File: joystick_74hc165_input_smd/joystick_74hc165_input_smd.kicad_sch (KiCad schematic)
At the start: 19 parts, among them J1 Conn_01x18, J2 Conn_02x14_Odd_Even

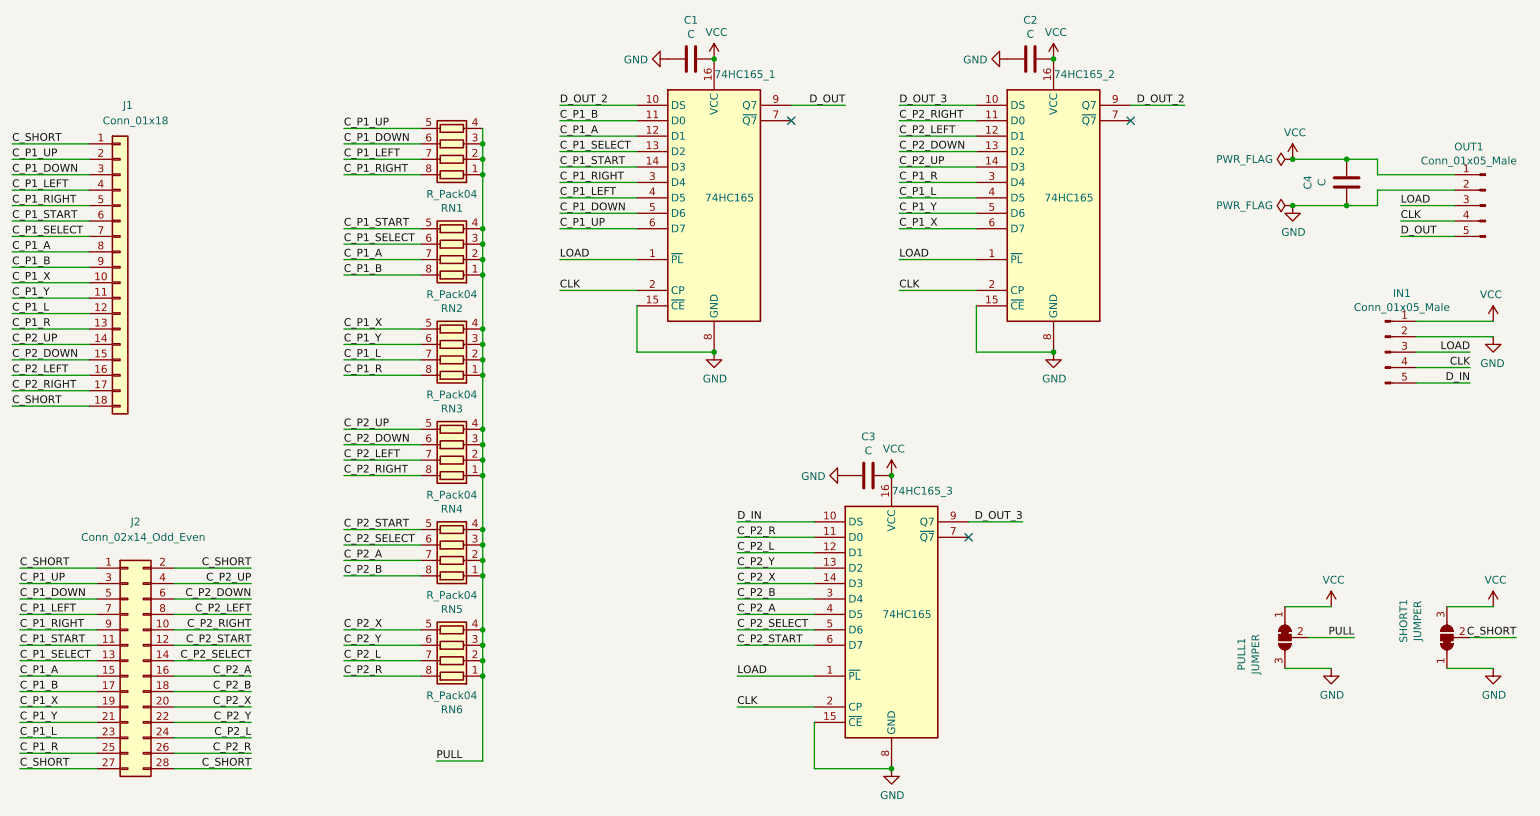
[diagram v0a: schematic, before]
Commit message: 부품 값 입력
Signed-off-by: Ju, Gyeong-min <jcmh74@gmail.com>
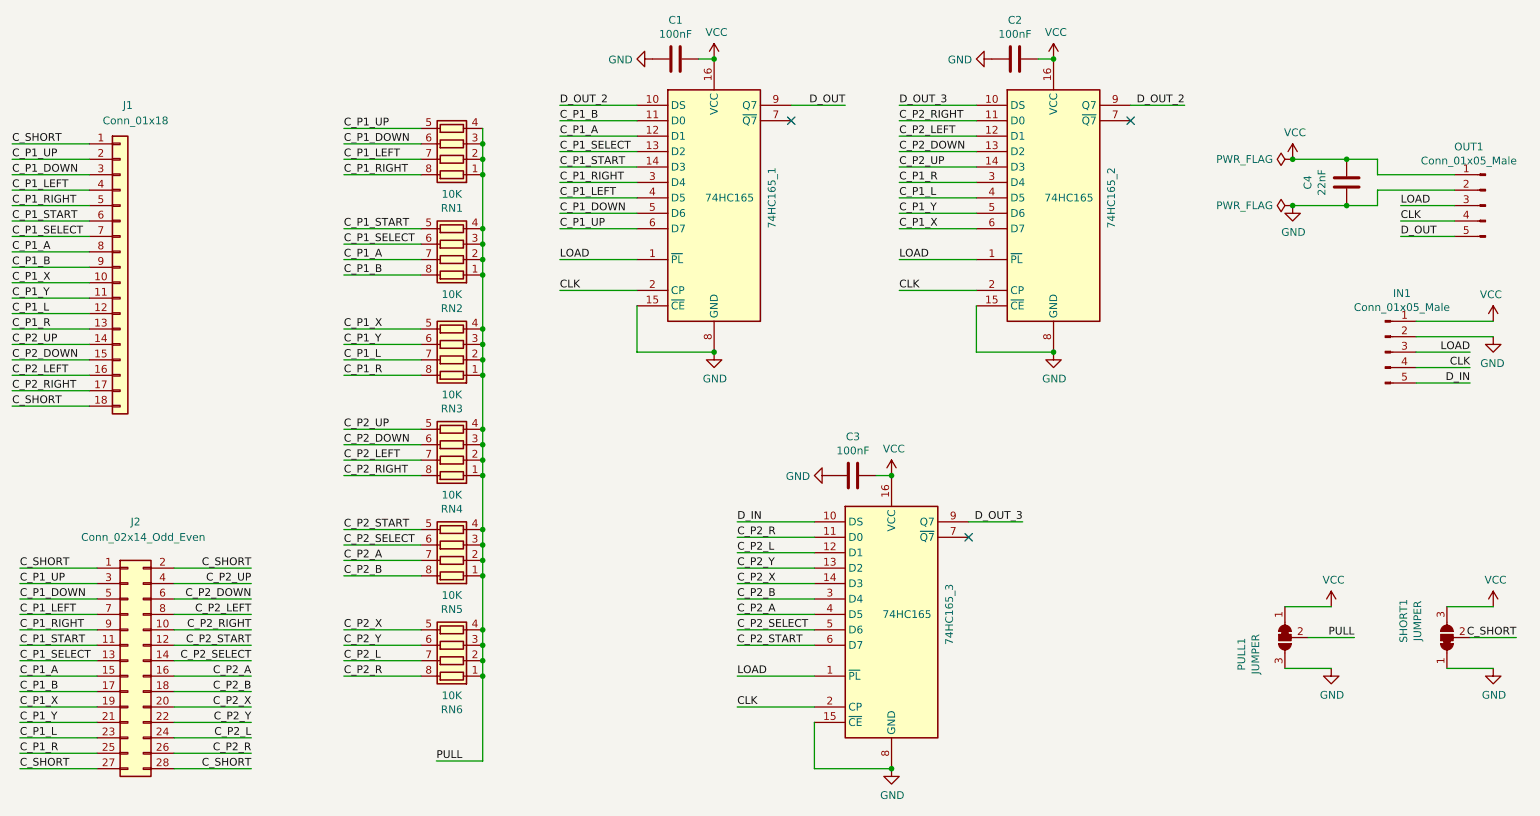
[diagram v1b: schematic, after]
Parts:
- C1, C2, C3: value C -> 100nF
- C4: value C -> 22nF
- RN1, RN2, RN3, RN4, RN5, RN6: value R_Pack04 -> 10K
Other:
- moved on the sheet: C1, C2, C3
